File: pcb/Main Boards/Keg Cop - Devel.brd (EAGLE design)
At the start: 65 x 51 mm, 27 parts

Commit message: Add proper value for R6
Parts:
- R6: value 2.2kΩ -> 200kΩ
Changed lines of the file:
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@@
 <attribute name="VALUE" x="60.205" y="35.949" size="1.27" layer="27" ratio="10"/>
 </element>
-<element name="R6" library="SparkFun-Resistors" library_urn="urn:adsk.eagle:library:532" package="AXIAL-0.3" package3d_urn="urn:adsk.eagle:package:39658/1" value="2.2kΩ" x="54.4" y="33.7" smashed="yes" rot="R180">
+<element name="R6" library="SparkFun-Resistors" library_urn="urn:adsk.eagle:library:532" package="AXIAL-0.3" package3d_urn="urn:adsk.eagle:package:39658/1" value="200kΩ" x="54.4" y="33.7" smashed="yes" rot="R180">
 <attribute name="NAME" x="54.4" y="34.784" size="0.8128" layer="25" font="vector" rot="R180" align="top-center"/>
 <attribute name="PROD_ID" value=" " x="54.4" y="33.7" size="1.778" layer="27" rot="R180" display="off"/>

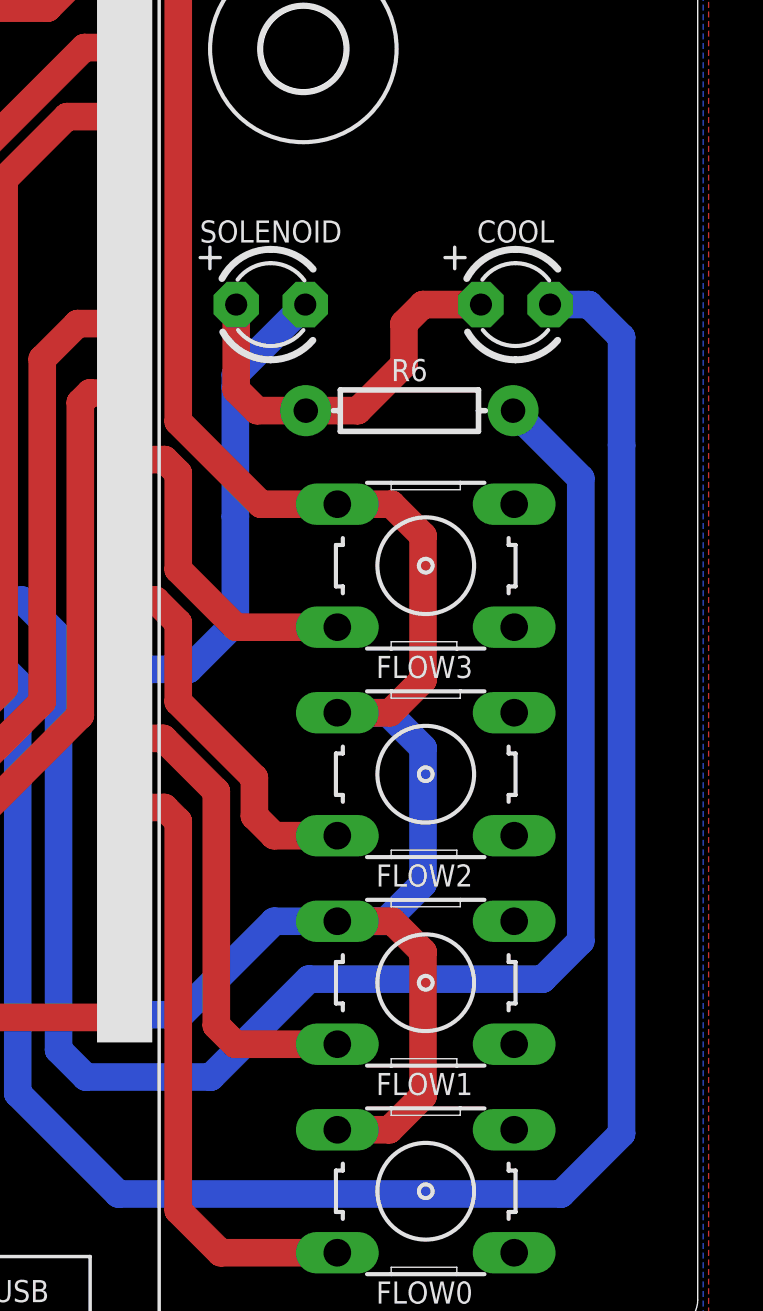
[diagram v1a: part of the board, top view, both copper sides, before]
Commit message: Add separate power for sol/cool
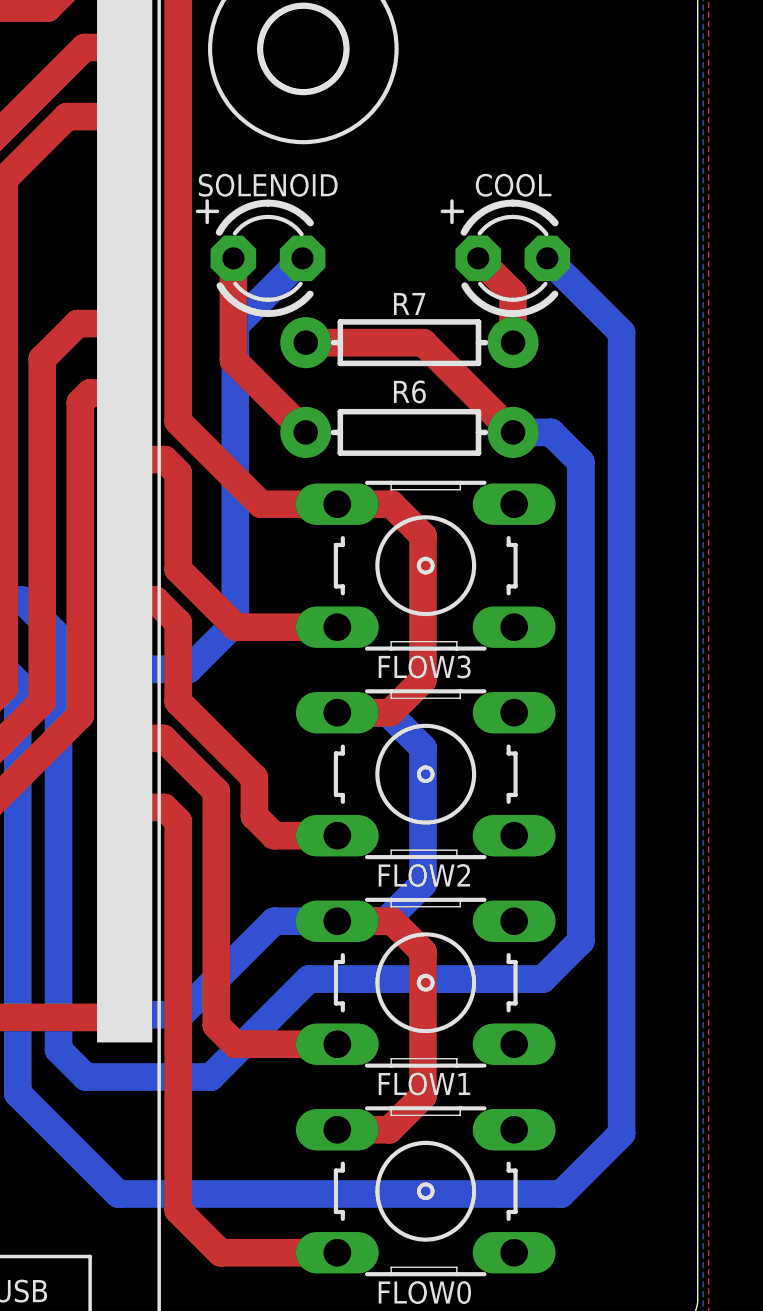
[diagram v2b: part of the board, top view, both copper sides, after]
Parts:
- added R7: 200kΩ, SparkFun-Resistors:AXIAL-0.3
- moved COOL 1.70 mm to (58.2, 39.3)
- moved SOLENOID 1.70 mm to (49.2, 39.3)
- moved R6 0.80 mm to (54.4, 32.9)
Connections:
- new net N$1: COOL.A, R7.P$2
- net 3V3: now also R7.P$1
- net N$2: no longer COOL.A
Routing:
- net 3V3: track 140.5 -> 149.5 mm
- net N$2: track 14.9 -> 7.50 mm
- net N$1: track 0.00 -> 3.63 mm
- net SOL: track 17.5 -> 19.2 mm
- net COOL: track 92.3 -> 93.2 mm
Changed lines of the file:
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@@
 <?xml version="1.0" encoding="utf-8"?>
 <!DOCTYPE eagle SYSTEM "eagle.dtd">
-<eagle version="9.5.2">
+<eagle version="9.6.2">
 <drawing>
 <settings>
@@
 <attribute name="VALUE" x="12.798" y="33.079996875" size="1.27" layer="27" ratio="10" rot="R180"/>
 </element>
-<element name="SOLENOID" library="adafruit" library_urn="urn:adsk.eagle:library:420" package="LED3MM" package3d_urn="urn:adsk.eagle:package:6240537/1" value="" x="49.3" y="37.6" smashed="yes">
-<attribute name="NAME" x="49.305" y="39.881" size="0.8128" layer="25" align="bottom-center"/>
-<attribute name="VALUE" x="51.205" y="35.949" size="1.27" layer="27" ratio="10"/>
-</element>
-<element name="COOL" library="adafruit" library_urn="urn:adsk.eagle:library:420" package="LED3MM" package3d_urn="urn:adsk.eagle:package:6240537/1" value="" x="58.3" y="37.6" smashed="yes">
-<attribute name="NAME" x="58.305" y="39.881" size="0.8128" layer="25" align="bottom-center"/>
-<attribute name="VALUE" x="60.205" y="35.949" size="1.27" layer="27" ratio="10"/>
-</element>
-<element name="R6" library="SparkFun-Resistors" library_urn="urn:adsk.eagle:library:532" package="AXIAL-0.3" package3d_urn="urn:adsk.eagle:package:39658/1" value="200kΩ" x="54.4" y="33.7" smashed="yes" rot="R180">
-<attribute name="NAME" x="54.4" y="34.784" size="0.8128" layer="25" font="vector" rot="R180" align="top-center"/>
-<attribute name="PROD_ID" value=" " x="54.4" y="33.7" size="1.778" layer="27" rot="R180" display="off"/>
+<element name="SOLENOID" library="adafruit" library_urn="urn:adsk.eagle:library:420" package="LED3MM" package3d_urn="urn:adsk.eagle:package:6240537/1" value="" x="49.2" y="39.3" smashed="yes">
+<attribute name="NAME" x="49.205" y="41.581" size="0.8128" layer="25" align="bottom-center"/>
+<attribute name="VALUE" x="51.105" y="37.649" size="1.27" layer="27" ratio="10"/>
+</element>
+<element name="COOL" library="adafruit" library_urn="urn:adsk.eagle:library:420" package="LED3MM" package3d_urn="urn:adsk.eagle:package:6240537/1" value="" x="58.2" y="39.3" smashed="yes">
+<attribute name="NAME" x="58.205" y="41.581" size="0.8128" layer="25" align="bottom-center"/>
+<attribute name="VALUE" x="60.105" y="37.649" size="1.27" layer="27" ratio="10"/>
+</element>
+<element name="R6" library="SparkFun-Resistors" library_urn="urn:adsk.eagle:library:532" package="AXIAL-0.3" package3d_urn="urn:adsk.eagle:package:39658/1" value="200kΩ" x="54.4" y="32.9" smashed="yes" rot="R180">
+<attribute name="NAME" x="54.4" y="33.984" size="0.8128" layer="25" font="vector" rot="R180" align="top-center"/>
+<attribute name="PROD_ID" value=" " x="54.4" y="32.9" size="1.778" layer="27" rot="R180" display="off"/>
 </element>
 <element name="KEG" library="SparkFun-Sensors" package="TO-92-AMMO" value="DS18B20" x="4.6" y="35.2" smashed="yes">
@@
 <element name="U$2" library="holes" library_urn="urn:adsk.eagle:library:237" package="3,0" package3d_urn="urn:adsk.eagle:package:14277/1" value="" x="14.5" y="47" smashed="yes"/>
 <element name="U$3" library="holes" library_urn="urn:adsk.eagle:library:237" package="3,0" package3d_urn="urn:adsk.eagle:package:14277/1" value="" x="32.5" y="4" smashed="yes"/>
+<element name="R7" library="SparkFun-Resistors" library_urn="urn:adsk.eagle:library:532" package="AXIAL-0.3" package3d_urn="urn:adsk.eagle:package:39658/1" value="200kΩ" x="54.4" y="36.2" smashed="yes">
+<attribute name="NAME" x="54.4" y="37.216" size="0.8128" layer="25" font="vector" align="bottom-center"/>
+<attribute name="PROD_ID" value=" " x="54.4" y="36.2" size="1.778" layer="27" display="off"/>
+</element>
 </elements>
 <signals>
@@
 <wire x1="32.36885" y1="45.703" x2="32.36385" y2="45.698" width="1.016" layer="1"/>
 <wire x1="22.81" y1="49.59" x2="21.07" y2="49.59" width="1.016" layer="1"/>
-<wire x1="60.7" y1="31.21" x2="60.7" y2="14.2" width="1.016" layer="16"/>
+<wire x1="60.7" y1="31.81" x2="60.7" y2="14.2" width="1.016" layer="16"/>
 <wire x1="59.3" y1="12.8" x2="60.7" y2="14.2" width="1.016" layer="16"/>
 <wire x1="50.7" y1="12.8" x2="47.1" y2="9.2" width="1.016" layer="16"/>
@@
 <wire x1="19.2" y1="42.56" x2="17.24" y2="40.6" width="1.016" layer="1"/>
 <wire x1="19.2" y1="47.72" x2="19.2" y2="42.56" width="1.016" layer="1"/>
-<wire x1="58.21" y1="33.7" x2="60.7" y2="31.21" width="1.016" layer="16"/>
+<contactref element="R7" pad="P$1"/>
+<wire x1="60.7" y1="31.81" x2="59.61" y2="32.9" width="1.016" layer="16"/>
+<wire x1="59.61" y1="32.9" x2="58.21" y2="32.9" width="1.016" layer="16"/>
+<wire x1="50.59" y1="36.2" x2="54.91" y2="36.2" width="1.016" layer="1"/>
+<wire x1="54.91" y1="36.2" x2="58.21" y2="32.9" width="1.016" layer="1"/>
 </signal>
 <signal name="GND">
@@
 <signal name="COOL">
 <contactref element="D32" pad="IO27"/>
-<wire x1="62.2" y1="7.12" x2="62.2" y2="32.43" width="1.016" layer="16"/>
 <wire x1="43.7" y1="4.9" x2="59.98" y2="4.9" width="1.016" layer="16"/>
 <wire x1="59.98" y1="4.9" x2="62.2" y2="7.12" width="1.016" layer="16"/>
@@
 <wire x1="40" y1="8.6" x2="43.7" y2="4.9" width="1.016" layer="16"/>
 <contactref element="COOL" pad="K"/>
-<wire x1="62.2" y1="32.43" x2="62.2" y2="36.4" width="1.016" layer="16"/>
-<wire x1="61" y1="37.6" x2="59.57" y2="37.6" width="1.016" layer="16"/>
-<wire x1="62.2" y1="36.4" x2="61" y2="37.6" width="1.016" layer="16"/>
+<wire x1="62.2" y1="7.12" x2="62.2" y2="36.57" width="1.016" layer="16"/>
+<wire x1="62.2" y1="36.57" x2="59.47" y2="39.3" width="1.016" layer="16"/>
 </signal>
 <signal name="SOL">
 <contactref element="D32" pad="IO16"/>
 <wire x1="43.93" y1="24.19" x2="46.29" y2="24.19" width="1.016" layer="16"/>
-<wire x1="48" y1="25.9" x2="48" y2="29.8" width="1.016" layer="16"/>
 <wire x1="46.29" y1="24.19" x2="48" y2="25.9" width="1.016" layer="16"/>
-<wire x1="48" y1="29.8" x2="48" y2="34.57" width="1.016" layer="16"/>
+<wire x1="48" y1="35.7" x2="48" y2="25.9" width="1.016" layer="16"/>
 <contactref element="SOLENOID" pad="K"/>
-<wire x1="48" y1="34.57" x2="48" y2="35.03" width="1.016" layer="16"/>
-<wire x1="48" y1="35.03" x2="50.57" y2="37.6" width="1.016" layer="16"/>
+<wire x1="50.47" y1="39.3" x2="48" y2="36.83" width="1.016" layer="16"/>
+<wire x1="48" y1="36.83" x2="48" y2="35.7" width="1.016" layer="16"/>
 </signal>
 <signal name="N$2">
 <contactref element="R6" pad="P$2"/>
 <contactref element="SOLENOID" pad="A"/>
+<wire x1="50.59" y1="32.9" x2="47.93" y2="35.56" width="1.016" layer="1"/>
+<wire x1="47.93" y1="35.56" x2="47.93" y2="39.3" width="1.016" layer="1"/>
+</signal>
+<signal name="N$1">
 <contactref element="COOL" pad="A"/>
-<wire x1="48.03" y1="37.6" x2="48.03" y2="34.47" width="1.016" layer="1"/>
-<wire x1="48.8" y1="33.7" x2="50.59" y2="33.7" width="1.016" layer="1"/>
-<wire x1="48.03" y1="34.47" x2="48.8" y2="33.7" width="1.016" layer="1"/>
-<wire x1="50.59" y1="33.7" x2="52.5" y2="33.7" width="1.016" layer="1"/>
-<wire x1="54.2" y1="35.4" x2="54.2" y2="36.9" width="1.016" layer="1"/>
-<wire x1="54.2" y1="36.9" x2="54.9" y2="37.6" width="1.016" layer="1"/>
-<wire x1="54.9" y1="37.6" x2="57.03" y2="37.6" width="1.016" layer="1"/>
-<wire x1="52.5" y1="33.7" x2="54.2" y2="35.4" width="1.016" layer="1"/>
+<contactref element="R7" pad="P$2"/>
+<wire x1="58.21" y1="36.2" x2="58.21" y2="38.02" width="1.016" layer="1"/>
+<wire x1="58.21" y1="38.02" x2="56.93" y2="39.3" width="1.016" layer="1"/>
 </signal>
 </signals>
